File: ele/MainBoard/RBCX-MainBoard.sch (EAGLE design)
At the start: 353 parts, among them IC1 DRV8833PWP, IC10 INA180A4, IC11 AMS1117-3.3, IC2 INA180A4, IC3 INA180A4, IC4 DRV8833PWP, IC5 INA180A4, IC6 INA180A4, IC7 INA180A4, IC8 INA180A4, IC9 INA180A4, Q1 CHOOSE_ME, Q10 CHOOSE_ME, Q2 CHOOSE_ME, Q3 CHOOSE_ME, Q4 CHOOSE_ME, Q5 CHOOSE_ME, Q6 CHOOSE_ME, Q7 CHOOSE_ME, Q8 CHOOSE_ME, Q9 CHOOSE_ME, U1 STM32F103VCT6, X0 POWER_IN, X1 M3B, X2 M4B, X3 M3B, X4 M4B, X5 POWER_OUT, Y1 3215_2P, Y2 5032/2P

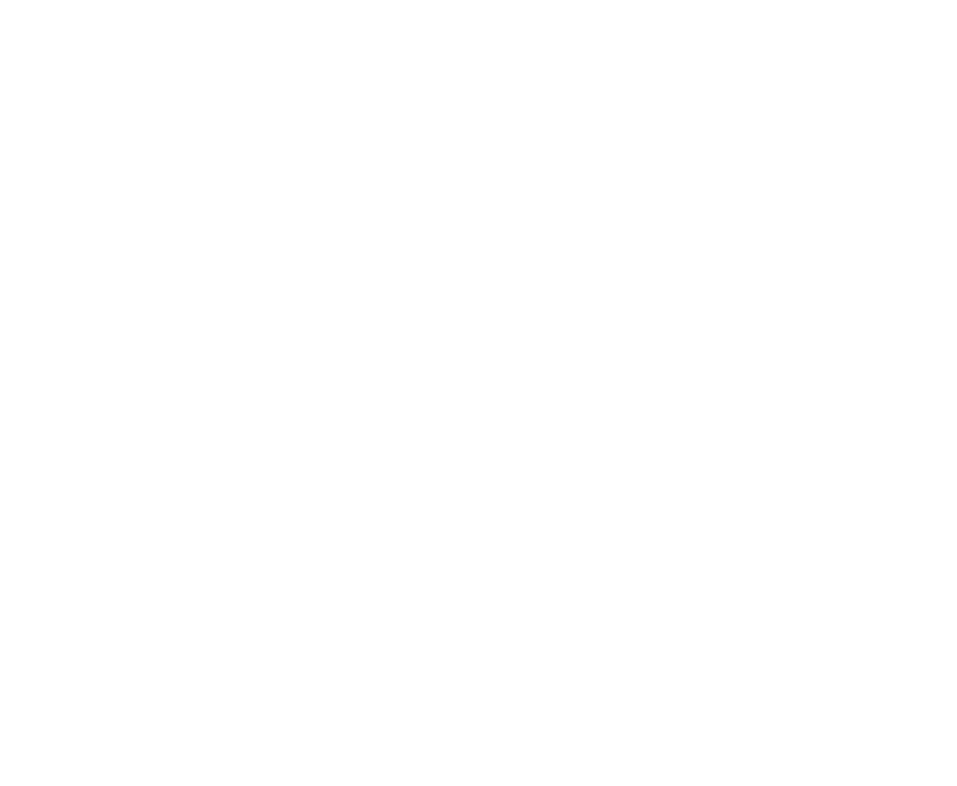
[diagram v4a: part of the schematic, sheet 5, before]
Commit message: MainBoardSCH: Add ESP UART and expander uart connector
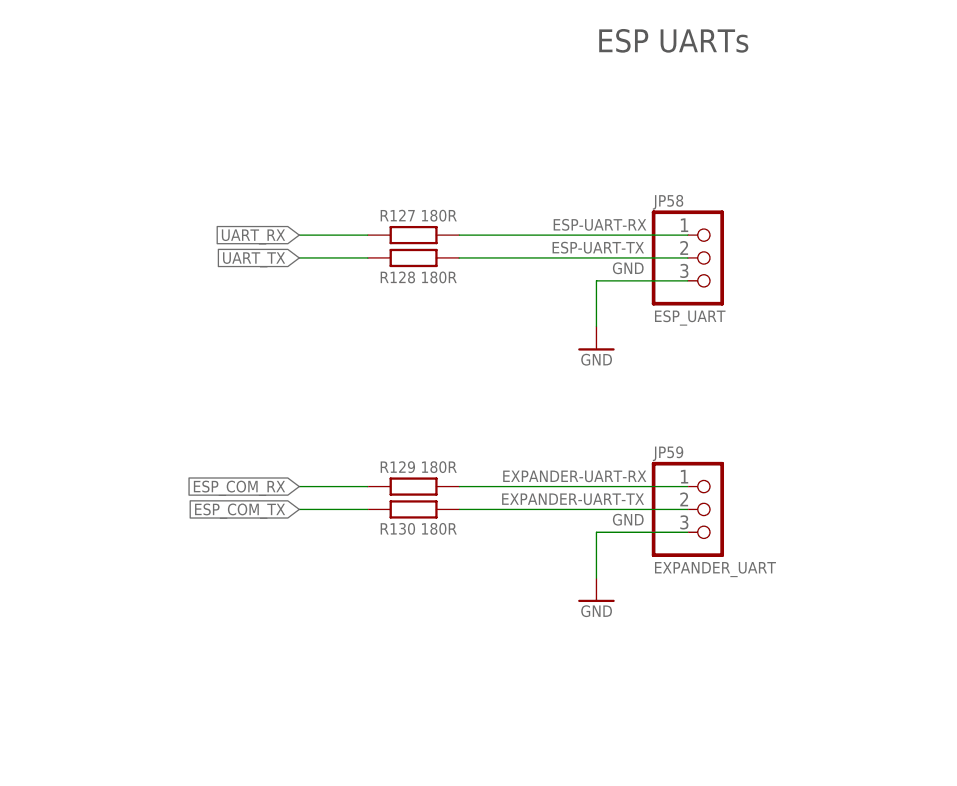
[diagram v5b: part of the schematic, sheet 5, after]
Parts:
- added JP58: ESP_UART, pinhead:PINHD-1X3
- added JP59: EXPANDER_UART, pinhead:PINHD-1X3
- added R127, R128, R129, R130: 180R, rcl_upravena:R-EU_R0603
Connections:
- new net ESP-UART-RX: JP58.1, R127.2
- new net ESP-UART-TX: JP58.2, R128.2
- new net EXPANDER-UART-RX: JP59.1, R129.2
- new net EXPANDER-UART-TX: JP59.2, R130.2
- net ESP_COM_RX: now also R129.1
- net ESP_COM_TX: now also R130.1
- net GND: now also JP58.3, JP59.3
- net UART_RX: now also R127.1
- net UART_TX: now also R128.1
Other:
- note added: "ESP UARTs"
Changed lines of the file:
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@@
 <attribute name="PRICE_DATE" value="17.03.2020"/>
 </part>
+<part name="JP58" library="pinhead" library_urn="urn:adsk.eagle:library:325" deviceset="PINHD-1X3" device="" package3d_urn="urn:adsk.eagle:package:22458/2" value="ESP_UART"/>
+<part name="GND157" library="Supply" deviceset="GND" device=""/>
+<part name="R127" library="rcl_upravena" deviceset="R-EU_" device="R0603" value="180R"/>
+<part name="R128" library="rcl_upravena" deviceset="R-EU_" device="R0603" value="180R"/>
+<part name="JP59" library="pinhead" library_urn="urn:adsk.eagle:library:325" deviceset="PINHD-1X3" device="" package3d_urn="urn:adsk.eagle:package:22458/2" value="EXPANDER_UART"/>
+<part name="GND158" library="Supply" deviceset="GND" device=""/>
+<part name="R129" library="rcl_upravena" deviceset="R-EU_" device="R0603" value="180R"/>
+<part name="R130" library="rcl_upravena" deviceset="R-EU_" device="R0603" value="180R"/>
 </parts>
 <sheets>
@@
 <text x="233.68" y="55.88" size="2.54" layer="97">ANALOG</text>
 <text x="93.98" y="121.92" size="2.54" layer="97">USB</text>
+<text x="345.44" y="246.38" size="2.54" layer="97">ESP UARTs</text>
 </plain>
 <instances>
@@
 <attribute name="VALUE" x="242.062" y="242.316" size="1.27" layer="96" rot="MR270"/>
 </instance>
+<instance part="JP58" gate="A" x="358.14" y="223.52" smashed="yes">
+<attribute name="NAME" x="351.79" y="229.235" size="1.27" layer="95"/>
+<attribute name="VALUE" x="351.79" y="217.678" size="1.27" layer="96" rot="MR180"/>
+</instance>
+<instance part="GND157" gate="1" x="345.44" y="213.36" smashed="yes">
+<attribute name="VALUE" x="343.662" y="211.582" size="1.27" layer="96"/>
+</instance>
+<instance part="R127" gate="G$1" x="325.12" y="226.06" smashed="yes">
+<attribute name="NAME" x="321.31" y="227.584" size="1.27" layer="95"/>
+<attribute name="VALUE" x="325.882" y="227.584" size="1.27" layer="96"/>
+</instance>
+<instance part="R128" gate="G$1" x="325.12" y="223.52" smashed="yes" rot="MR180">
+<attribute name="NAME" x="321.31" y="221.996" size="1.27" layer="95" rot="MR180"/>
+<attribute name="VALUE" x="325.882" y="221.996" size="1.27" layer="96" rot="MR180"/>
+</instance>
+<instance part="JP59" gate="A" x="358.14" y="195.58" smashed="yes">
+<attribute name="NAME" x="351.79" y="201.295" size="1.27" layer="95"/>
+<attribute name="VALUE" x="351.79" y="189.738" size="1.27" layer="96" rot="MR180"/>
+</instance>
+<instance part="GND158" gate="1" x="345.44" y="185.42" smashed="yes">
+<attribute name="VALUE" x="343.662" y="183.642" size="1.27" layer="96"/>
+</instance>
+<instance part="R129" gate="G$1" x="325.12" y="198.12" smashed="yes">
+<attribute name="NAME" x="321.31" y="199.644" size="1.27" layer="95"/>
+<attribute name="VALUE" x="325.882" y="199.644" size="1.27" layer="96"/>
+</instance>
+<instance part="R130" gate="G$1" x="325.12" y="195.58" smashed="yes" rot="MR180">
+<attribute name="NAME" x="321.31" y="194.056" size="1.27" layer="95" rot="MR180"/>
+<attribute name="VALUE" x="325.882" y="194.056" size="1.27" layer="96" rot="MR180"/>
+</instance>
 </instances>
 <busses>
@@
 <wire x1="53.34" y1="55.88" x2="53.34" y2="58.42" width="0.1524" layer="91"/>
 </segment>
+<segment>
+<pinref part="JP58" gate="A" pin="3"/>
+<pinref part="GND157" gate="1" pin="GND"/>
+<wire x1="355.6" y1="220.98" x2="345.44" y2="220.98" width="0.1524" layer="91"/>
+<wire x1="345.44" y1="220.98" x2="345.44" y2="215.9" width="0.1524" layer="91"/>
+<label x="350.774" y="221.742" size="1.27" layer="95" rot="MR0"/>
+</segment>
+<segment>
+<pinref part="JP59" gate="A" pin="3"/>
+<pinref part="GND158" gate="1" pin="GND"/>
+<wire x1="355.6" y1="193.04" x2="345.44" y2="193.04" width="0.1524" layer="91"/>
+<wire x1="345.44" y1="193.04" x2="345.44" y2="187.96" width="0.1524" layer="91"/>
+<label x="350.774" y="193.802" size="1.27" layer="95" rot="MR0"/>
+</segment>
 </net>
 <net name="UTS1_TRIG" class="0">
@@
 </segment>
 </net>
+<net name="ESP-UART-RX" class="0">
+<segment>
+<pinref part="R127" gate="G$1" pin="2"/>
+<pinref part="JP58" gate="A" pin="1"/>
+<wire x1="330.2" y1="226.06" x2="355.6" y2="226.06" width="0.1524" layer="91"/>
+<label x="351.028" y="226.568" size="1.27" layer="95" rot="MR0"/>
+</segment>
+</net>
+<net name="ESP-UART-TX" class="0">
+<segment>
+<pinref part="R128" gate="G$1" pin="2"/>
+<pinref part="JP58" gate="A" pin="2"/>
+<wire x1="330.2" y1="223.52" x2="355.6" y2="223.52" width="0.1524" layer="91"/>
+<label x="350.774" y="224.028" size="1.27" layer="95" rot="MR0"/>
+</segment>
+</net>
+<net name="UART_TX" class="0">
+<segment>
+<pinref part="R128" gate="G$1" pin="1"/>
+<wire x1="320.04" y1="223.52" x2="312.42" y2="223.52" width="0.1524" layer="91"/>
+<label x="312.42" y="223.52" size="1.27" layer="95" rot="R180" xref="yes"/>
+</segment>
+</net>
+<net name="UART_RX" class="0">
+<segment>
+<pinref part="R127" gate="G$1" pin="1"/>
+<wire x1="320.04" y1="226.06" x2="312.42" y2="226.06" width="0.1524" layer="91"/>
+<label x="312.42" y="226.06" size="1.27" layer="95" rot="R180" xref="yes"/>
+</segment>
+</net>
+<net name="EXPANDER-UART-RX" class="0">
+<segment>
+<pinref part="R129" gate="G$1" pin="2"/>
+<pinref part="JP59" gate="A" pin="1"/>
+<wire x1="330.2" y1="198.12" x2="355.6" y2="198.12" width="0.1524" layer="91"/>
+<label x="351.028" y="198.628" size="1.27" layer="95" rot="MR0"/>
+</segment>
+</net>
+<net name="EXPANDER-UART-TX" class="0">
+<segment>
+<pinref part="R130" gate="G$1" pin="2"/>
+<pinref part="JP59" gate="A" pin="2"/>
+<wire x1="330.2" y1="195.58" x2="355.6" y2="195.58" width="0.1524" layer="91"/>
+<label x="350.774" y="196.088" size="1.27" layer="95" rot="MR0"/>
+</segment>
+</net>
+<net name="ESP_COM_RX" class="0">
+<segment>
+<pinref part="R129" gate="G$1" pin="1"/>
+<wire x1="320.04" y1="198.12" x2="312.42" y2="198.12" width="0.1524" layer="91"/>
+<label x="312.42" y="198.12" size="1.27" layer="95" rot="R180" xref="yes"/>
+</segment>
+</net>
+<net name="ESP_COM_TX" class="0">
+<segment>
+<pinref part="R130" gate="G$1" pin="1"/>
+<wire x1="320.04" y1="195.58" x2="312.42" y2="195.58" width="0.1524" layer="91"/>
+<label x="312.42" y="195.58" size="1.27" layer="95" rot="R180" xref="yes"/>
+</segment>
+</net>

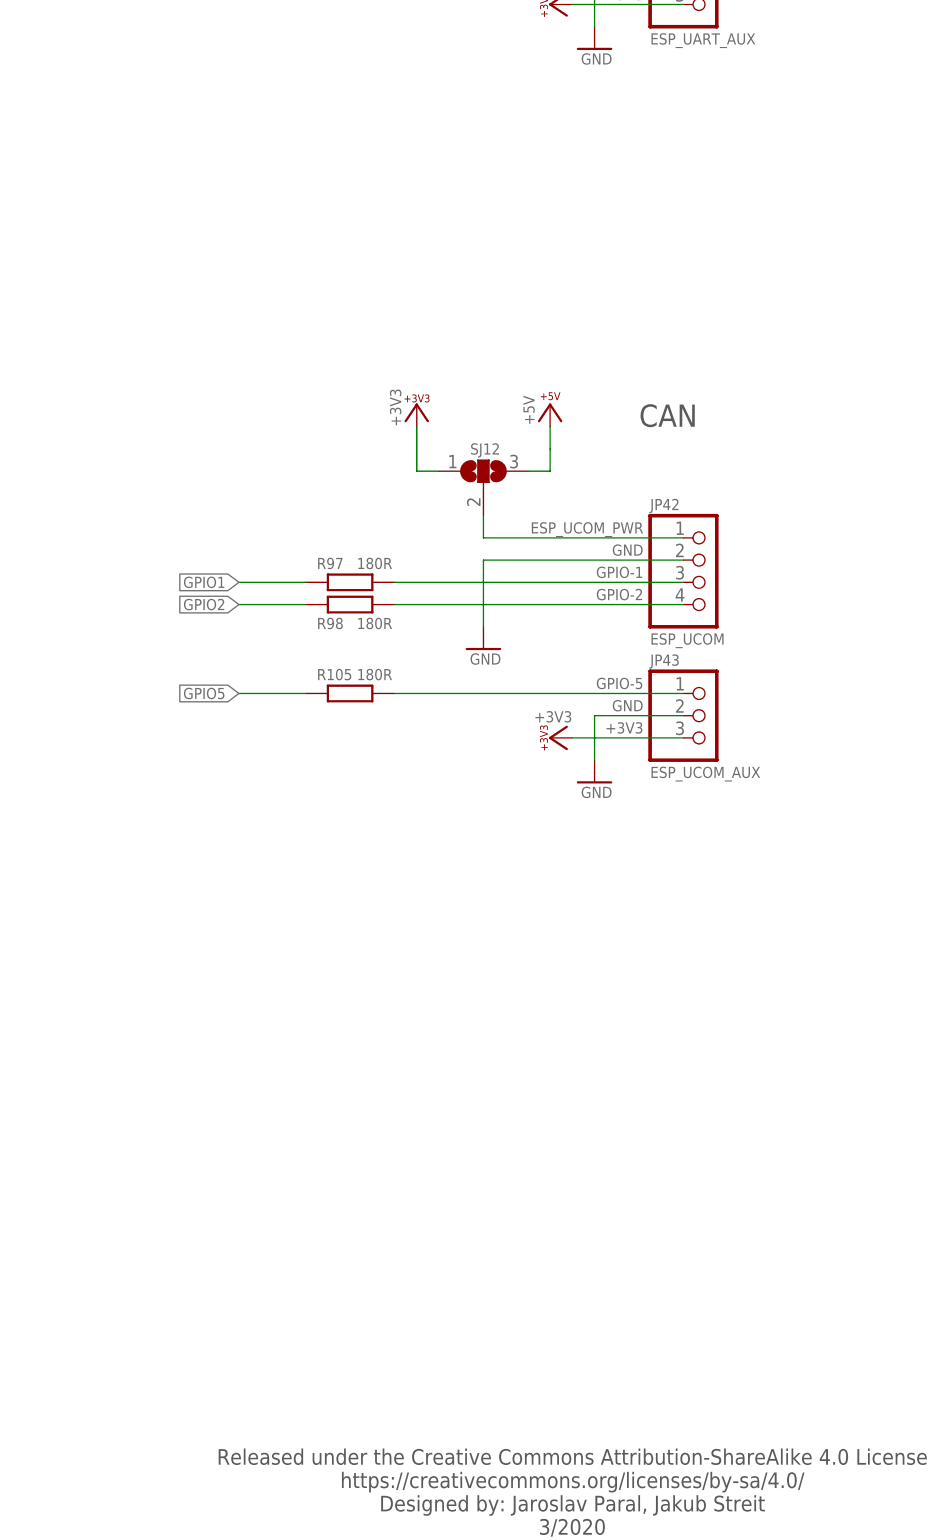
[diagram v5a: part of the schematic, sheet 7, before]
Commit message: MainBoardSCH: Add power connectors
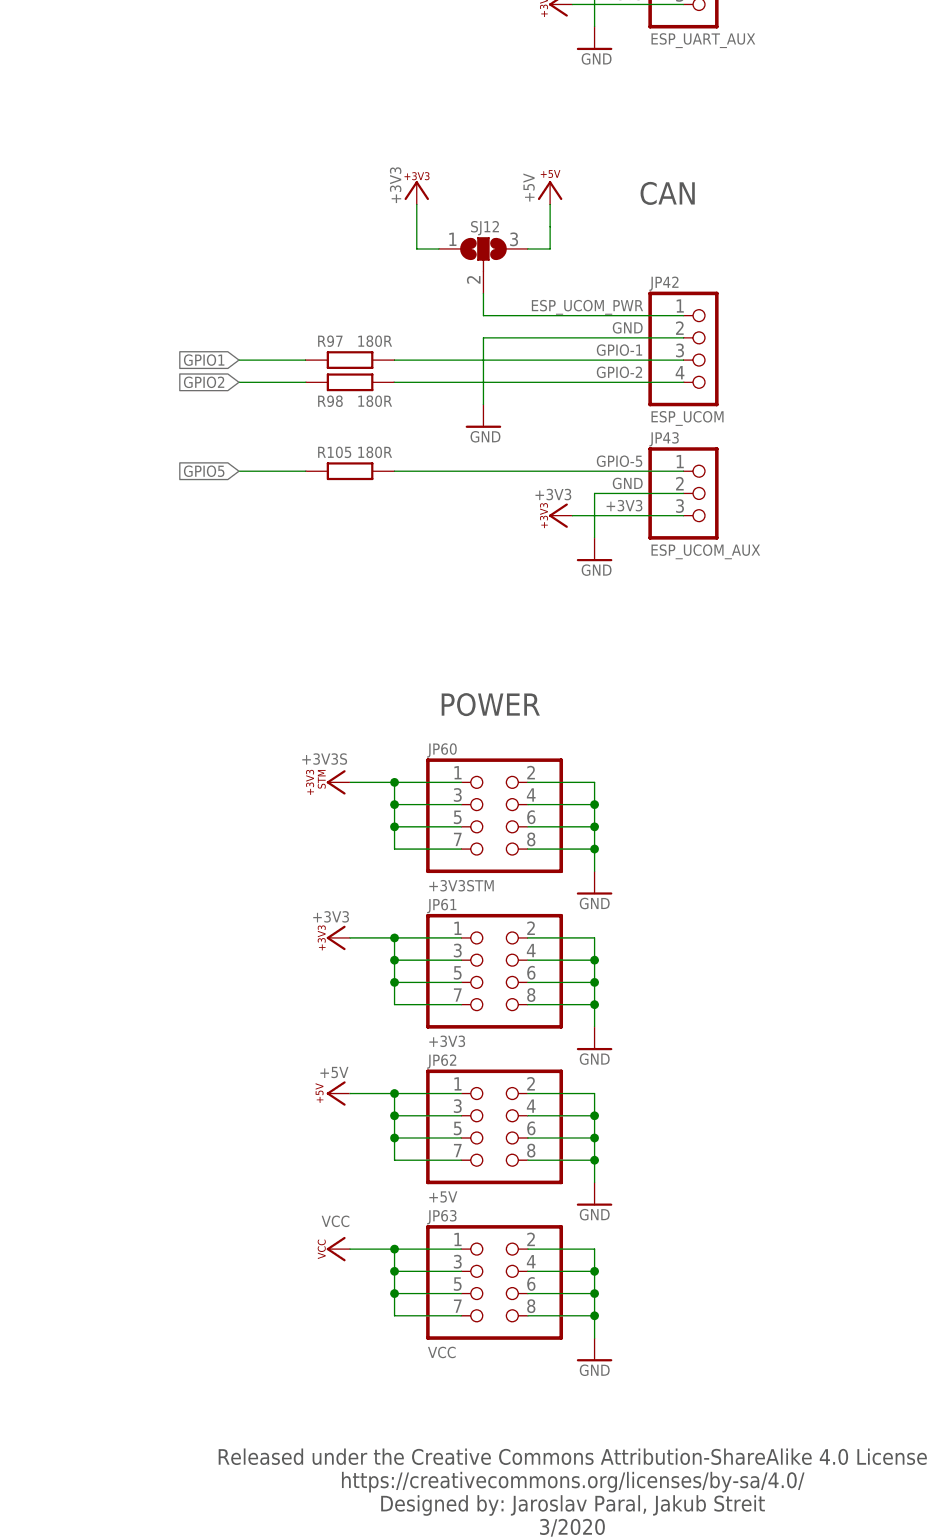
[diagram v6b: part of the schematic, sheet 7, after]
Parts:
- added JP60: +3V3STM, pinhead:PINHD-2X4
- added JP61: +3V3, pinhead:PINHD-2X4
- added JP62: +5V, pinhead:PINHD-2X4
- added JP63: VCC, pinhead:PINHD-2X4
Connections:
- net +3V3: now also JP61.1, JP61.3, JP61.5, JP61.7
- net +3V3S: now also JP60.1, JP60.3, JP60.5, JP60.7
- net +5V: now also JP62.1, JP62.3, JP62.5, JP62.7
- net GND: now also JP60.2, JP60.4, JP60.6, JP60.8, JP61.2, JP61.4, JP61.6, JP61.8, JP62.2, JP62.4, JP62.6, JP62.8, JP63.2, JP63.4, JP63.6, JP63.8
- net VCC: now also JP63.1, JP63.3, JP63.5, JP63.7
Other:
- note added: "POWER"
- moved on the sheet: JP42, JP43, R105, R97, R98, SJ12
